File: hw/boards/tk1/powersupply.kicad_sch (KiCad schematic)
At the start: 19 parts

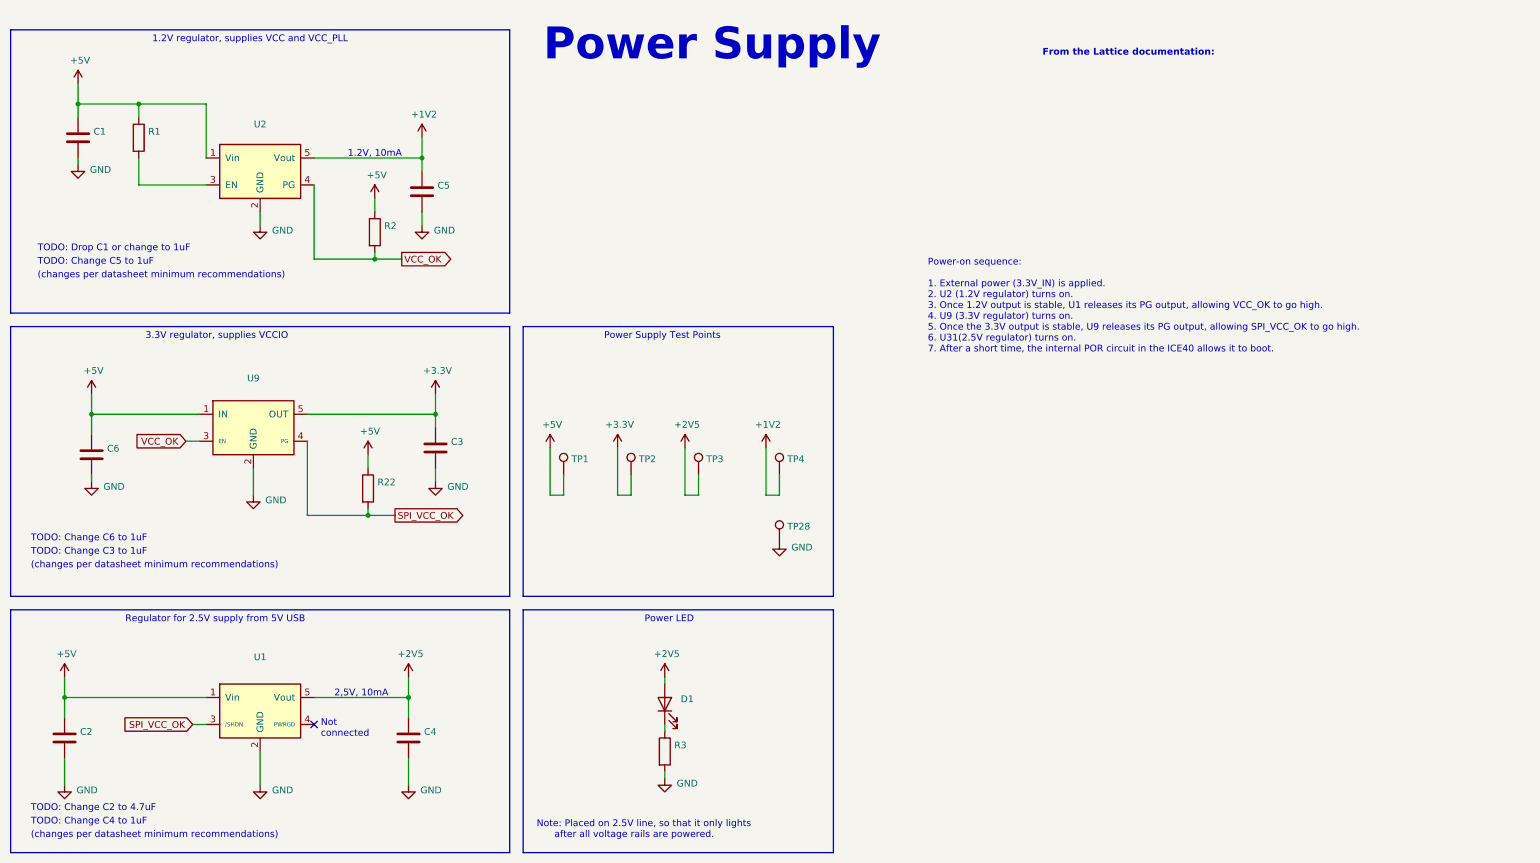
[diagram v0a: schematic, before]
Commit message: TK-1 and TP-1 PCBs (#52)
* Add kicad library for flat programming clip

* Add descriptions to part symbols

* Add extended values, manufacturer/distributor info to components in mta1

* Add new board entry for TK1

* Add TP1 programmer design

* Update MTA1-USB-V1 release files to match production

* Change SPI flash memory type to XT25F08BDFIGT-S
* Change touch sensor feedback cap to 1uF
* Add manufacturer, manufacturer part number, distributor, distributor part number

* Update component values for TK1 PCB

* Use specific part # for C8
* Change flash back to Winbond part, for easier sourcing
* Change C1 to 1pF

* Fixes for production programmer PCB

* Swap GND and 5V on J3
* Replace graphic logo with text
* Rename part to 'TP-1'

* TK-1 release

* Add dimensions for PCB
* Add layer stackup for PCB
* Change PCB component origin to match expanded board
* Change schematic title to 'TK-1', update release date

* mta1-usb-v1-programmer: Add corrected part numbers for OSFC production

* Q1, Q2, F1 part subsititutions
* add mfr/supplier info for all parts

* PCB library: add parts

* Rectangular footprint for TK-1 test pads
* BOM generation script used for TK-1 and TP-1 releases

* TP-1 release

* Schematic: Add manufacturer, supplier information for all parts
* Schematic: Update name and release date
* PCB: Add PCB fabrication information
* PCB: Correct pinouts on silkscreen

* PCB library: add 'screw' and 'foot' symbols

* Screw is a schematic-only part, for including mechanical screws in the
  BOM
* Foot is for self-adhesive rubber mounting feet that can be stuck to
  the bottom of a PCB

* TP-1 release: Add screws, feet to the BOM

* Pico library: Add footprint for RPi Pico w/solder paste

* TP-1 RevA release updates:

* Add fiducials in 3 corners (1mm exposed copper ring w/2mm soldermask opening)
* Add solder paste openings to Raspberry Pi Pico pads

* TK-1: RevA.1 release

* Add two fiducials to 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
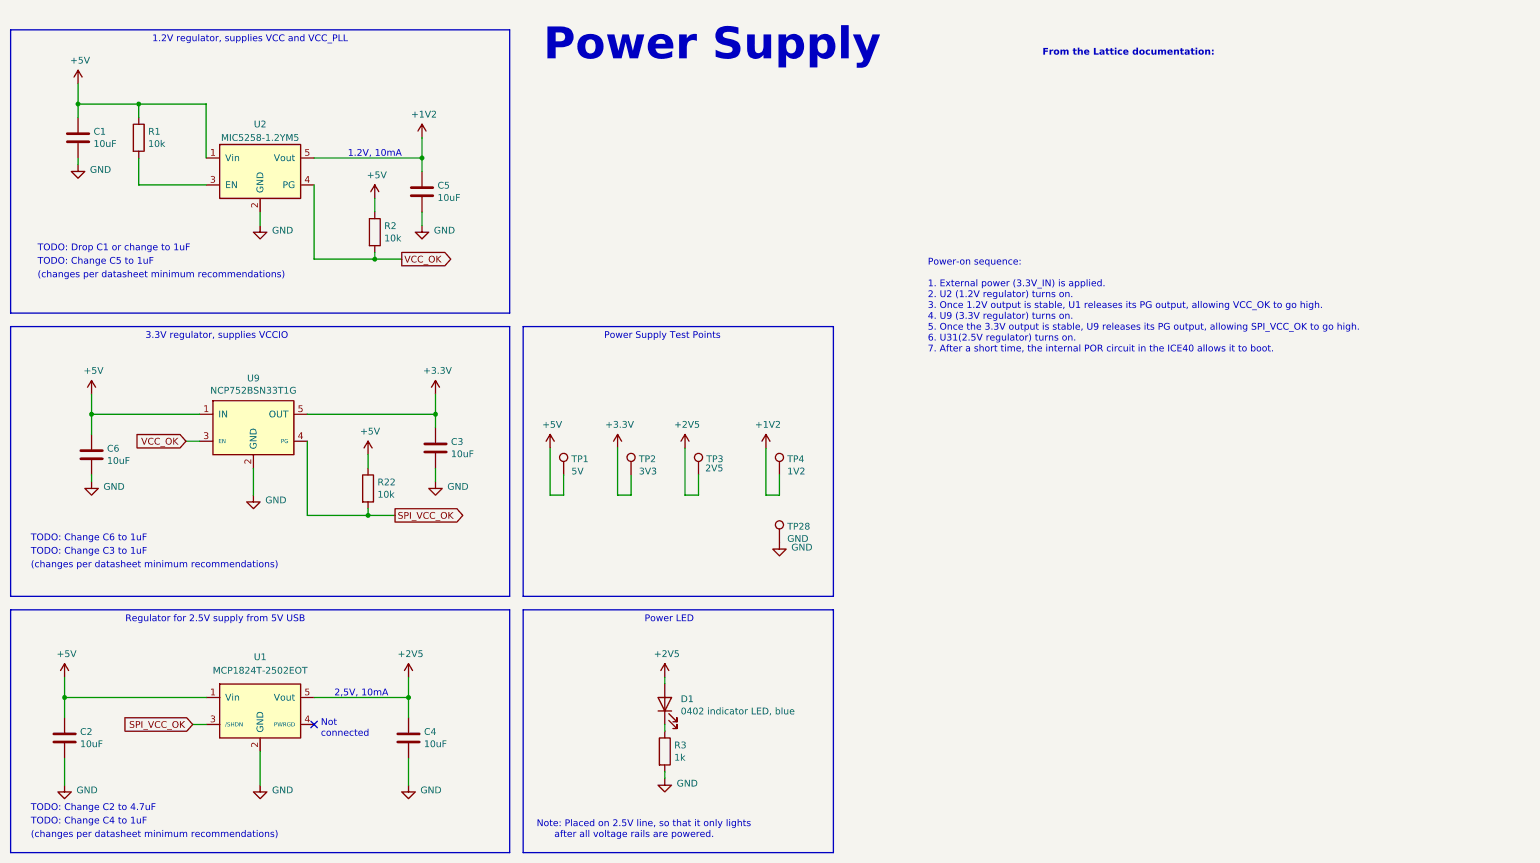
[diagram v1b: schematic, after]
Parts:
- C1, C2, C3, C4, C5, C6: value (none) -> 10uF; footprint (none) -> mta1:CAPC1608X09L
- D1: value (none) -> 0402 indicator LED, blue; footprint (none) -> LED_SMD:LED_0402_1005Metric
- R1, R2, R22: value (none) -> 10k; footprint (none) -> mta1:ERJ2G(0402)_L
- R3: value (none) -> 1k; footprint (none) -> mta1:ERJ2G(0402)_L
- TP1: value (none) -> 5V; footprint (none) -> mta1:TestPoint_Pad_D1.0mm
- TP2: value (none) -> 3V3; footprint (none) -> mta1:TestPoint_Pad_D1.0mm
- TP28: value (none) -> GND; footprint (none) -> mta1:TestPoint_Pad_D1.0mm
- TP3: value (none) -> 2V5; footprint (none) -> mta1:TestPoint_Pad_D1.0mm
- TP4: value (none) -> 1V2; footprint (none) -> mta1:TestPoint_Pad_D1.0mm
- U1: value (none) -> MCP1824T-2502EOT; footprint (none) -> Package_TO_SOT_SMD:SOT-23-5
- U2: value (none) -> MIC5258-1.2YM5; footprint (none) -> Package_TO_SOT_SMD:SOT-23-5
- U9: value (none) -> NCP752BSN33T1G; footprint (none) -> mta1:NCP752BSN33T1G
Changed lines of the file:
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@@
   (title_block
     (title "Power Supply")
-    (date "2021-09-29")
+    (date "2021-11-14")
     (rev "V1")
     (company "Tillitis AB")
@@
       (effects (font (size 1.27 1.27)) (justify left))
     )
-    (property "Value" "" (id 1) (at 33.401 39.243 0)
+    (property "Value" "10uF" (id 1) (at 33.401 39.243 0)
       (effects (font (size 1.27 1.27)) (justify left))
     )
-    (property "Footprint" "" (id 2) (at 31.4452 41.91 0)
+    (property "Footprint" "mta1:CAPC1608X09L" (id 2) (at 31.4452 41.91 0)
       (effects (font (size 1.27 1.27)) hide)
     )
@@
       (effects (font (size 1.27 1.27)) (justify left))
     )
-    (property "Value" "" (id 1) (at 43.688 39.243 0)
+    (property "Value" "10k" (id 1) (at 43.688 39.243 0)
       (effects (font (size 1.27 1.27)) (justify left))
     )
-    (property "Footprint" "" (id 2) (at 40.132 38.1 90)
+    (property "Footprint" "mta1:ERJ2G(0402)_L" (id 2) (at 40.132 38.1 90)
       (effects (font (size 1.27 1.27)) hide)
     )
@@
       (effects (font (size 1.27 1.27)) (justify left))
     )
-    (property "Value" "" (id 1) (at 98.171 49.403 0)
+    (property "Value" "10uF" (id 1) (at 98.171 49.403 0)
       (effects (font (size 1.27 1.27)) (justify left))
     )
-    (property "Footprint" "" (id 2) (at 96.2152 52.07 0)
+    (property "Footprint" "mta1:CAPC1608X09L" (id 2) (at 96.2152 52.07 0)
       (effects (font (size 1.27 1.27)) hide)
     )
@@
       (effects (font (size 1.27 1.27)) (justify left))
     )
-    (property "Value" "" (id 1) (at 88.138 57.023 0)
+    (property "Value" "10k" (id 1) (at 88.138 57.023 0)
       (effects (font (size 1.27 1.27)) (justify left))
     )
-    (property "Footprint" "" (id 2) (at 84.582 55.88 90)
+    (property "Footprint" "mta1:ERJ2G(0402)_L" (id 2) (at 84.582 55.88 90)
       (effects (font (size 1.27 1.27)) hide)
     )
@@
       (effects (font (size 1.27 1.27)) (justify left))
     )
-    (property "Value" "" (id 1) (at 100.711 97.663 0)
+    (property "Value" "10uF" (id 1) (at 100.711 97.663 0)
       (effects (font (size 1.27 1.27)) (justify left))
     )
-    (property "Footprint" "" (id 2) (at 98.7552 100.33 0)
+    (property "Footprint" "mta1:CAPC1608X09L" (id 2) (at 98.7552 100.33 0)
       (effects (font (size 1.27 1.27)) hide)
     )
@@
     (in_bom yes) (on_board yes)
     (property "Reference" "U2" (id 0) (at 64.77 35.56 0))
-    (property "Value" "" (id 1) (at 64.77 38.1 0))
-    (property "Footprint" "" (id 2) (at 64.77 34.29 0)
+    (property "Value" "MIC5258-1.2YM5" (id 1) (at 64.77 38.1 0))
+    (property "Footprint" "Package_TO_SOT_SMD:SOT-23-5" (id 2) (at 64.77 34.29 0)
       (effects (font (size 1.27 1.27)) hide)
     )
@@
     (in_bom yes) (on_board yes)
     (property "Reference" "U1" (id 0) (at 64.77 135.89 0))
-    (property "Value" "" (id 1) (at 64.77 138.43 0))
-    (property "Footprint" "" (id 2) (at 83.82 156.21 0)
+    (property "Value" "MCP1824T-2502EOT" (id 1) (at 64.77 138.43 0))
+    (property "Footprint" "Package_TO_SOT_SMD:SOT-23-5" (id 2) (at 83.82 156.21 0)
       (effects (font (size 1.27 1.27)) hide)
     )
@@
       (effects (font (size 1.27 1.27)) (justify left))
     )
-    (property "Value" "" (id 1) (at 30.861 152.273 0)
+    (property "Value" "10uF" (id 1) (at 30.861 152.273 0)
       (effects (font (size 1.27 1.27)) (justify left))
     )
-    (property "Footprint" "" (id 2) (at 28.9052 154.94 0)
+    (property "Footprint" "mta1:CAPC1608X09L" (id 2) (at 28.9052 154.94 0)
       (effects (font (size 1.27 1.27)) hide)
     )
@@
       (effects (font (size 1.27 1.27)) (justify left))
     )
-    (property "Value" "" (id 1) (at 95.631 152.273 0)
+    (property "Value" "10uF" (id 1) (at 95.631 152.273 0)
       (effects (font (size 1.27 1.27)) (justify left))
     )
-    (property "Footprint" "" (id 2) (at 93.6752 154.94 0)
+    (property "Footprint" "mta1:CAPC1608X09L" (id 2) (at 93.6752 154.94 0)
       (effects (font (size 1.27 1.27)) hide)
     )
@@
       (effects (font (size 1.27 1.27)) (justify left))
     )
-    (property "Value" "" (id 1) (at 136.0932 100.9142 0)
+    (property "Value" "3V3" (id 1) (at 136.0932 100.9142 0)
       (effects (font (size 1.27 1.27)) (justify left))
     )
-    (property "Footprint" "" (id 2) (at 139.7 101.6 0)
+    (property "Footprint" "mta1:TestPoint_Pad_D1.0mm" (id 2) (at 139.7 101.6 0)
       (effects (font (size 1.27 1.27)) hide)
     )
@@
       (effects (font (size 1.27 1.27)) (justify left))
     )
-    (property "Value" "" (id 1) (at 148.59 100.33 0)
+    (property "Value" "2V5" (id 1) (at 148.59 100.33 0)
       (effects (font (size 1.27 1.27)) (justify left))
     )
-    (property "Footprint" "" (id 2) (at 152.4 101.6 0)
+    (property "Footprint" "mta1:TestPoint_Pad_D1.0mm" (id 2) (at 152.4 101.6 0)
       (effects (font (size 1.27 1.27)) hide)
     )
@@
       (effects (font (size 1.27 1.27)) (justify left))
     )
-    (property "Value" "" (id 1) (at 164.0332 100.9142 0)
+    (property "Value" "1V2" (id 1) (at 164.0332 100.9142 0)
       (effects (font (size 1.27 1.27)) (justify left))
     )
-    (property "Footprint" "" (id 2) (at 167.64 101.6 0)
+    (property "Footprint" "mta1:TestPoint_Pad_D1.0mm" (id 2) (at 167.64 101.6 0)
       (effects (font (size 1.27 1.27)) hide)
     )
@@
     (in_bom yes) (on_board yes)
     (property "Reference" "U9" (id 0) (at 63.5 83.3882 0))
-    (property "Value" "" (id 1) (at 63.5 85.6996 0))
-    (property "Footprint" "" (id 2) (at 63.5 83.82 0)
+    (property "Value" "NCP752BSN33T1G" (id 1) (at 63.5 85.6996 0))
+    (property "Footprint" "mta1:NCP752BSN33T1G" (id 2) (at 63.5 83.82 0)
       (effects (font (size 1.27 1.27)) hide)
     )
@@
       (effects (font (size 1.27 1.27)) (justify left))
     )
-    (property "Value" "" (id 1) (at 35.941 98.933 0)
+    (property "Value" "10uF" (id 1) (at 35.941 98.933 0)
       (effects (font (size 1.27 1.27)) (justify left))
     )
-    (property "Footprint" "" (id 2) (at 33.9852 101.6 0)
+    (property "Footprint" "mta1:CAPC1608X09L" (id 2) (at 33.9852 101.6 0)
       (effects (font (size 1.27 1.27)) hide)
     )
@@
       (effects (font (size 1.27 1.27)) (justify left))
     )
-    (property "Value" "" (id 1) (at 142.748 154.813 0)
+    (property "Value" "1k" (id 1) (at 142.748 154.813 0)
       (effects (font (size 1.27 1.27)) (justify left))
     )
-    (property "Footprint" "" (id 2) (at 139.192 153.67 90)
+    (property "Footprint" "mta1:ERJ2G(0402)_L" (id 2) (at 139.192 153.67 90)
       (effects (font (size 1.27 1.27)) hide)
     )
@@
       (effects (font (size 1.27 1.27)) (justify right))
     )
-    (property "Value" "" (id 1) (at 143.9672 146.1008 90)
+    (property "Value" "0402 indicator LED, blue" (id 1) (at 143.9672 146.1008 90)
       (effects (font (size 1.27 1.27)) (justify right))
     )
-    (property "Footprint" "" (id 2) (at 140.97 144.78 0)
+    (property "Footprint" "LED_SMD:LED_0402_1005Metric" (id 2) (at 140.97 144.78 0)
       (effects (font (size 1.27 1.27)) hide)
     )
@@
       (effects (font (size 1.27 1.27)) (justify left))
     )
-    (property "Value" "" (id 1) (at 123.3932 100.9142 0)
+    (property "Value" "5V" (id 1) (at 123.3932 100.9142 0)
       (effects (font (size 1.27 1.27)) (justify left))
     )
-    (property "Footprint" "" (id 2) (at 127 101.6 0)
+    (property "Footprint" "mta1:TestPoint_Pad_D1.0mm" (id 2) (at 127 101.6 0)
       (effects (font (size 1.27 1.27)) hide)
     )
@@
       (effects (font (size 1.27 1.27)) (justify left))
     )
-    (property "Value" "" (id 1) (at 86.868 105.283 0)
+    (property "Value" "10k" (id 1) (at 86.868 105.283 0)
       (effects (font (size 1.27 1.27)) (justify left))
     )
-    (property "Footprint" "" (id 2) (at 83.312 104.14 90)
+    (property "Footprint" "mta1:ERJ2G(0402)_L" (id 2) (at 83.312 104.14 90)
       (effects (font (size 1.27 1.27)) hide)
     )
@@
       (effects (font (size 1.27 1.27)) (justify left))
     )
-    (property "Value" "" (id 1) (at 164.0332 113.6142 0)
+    (property "Value" "GND" (id 1) (at 164.0332 113.6142 0)
       (effects (font (size 1.27 1.27)) (justify left))
     )
-    (property "Footprint" "" (id 2) (at 167.64 114.3 0)
+    (property "Footprint" "mta1:TestPoint_Pad_D1.0mm" (id 2) (at 167.64 114.3 0)
       (effects (font (size 1.27 1.27)) hide)
     )
